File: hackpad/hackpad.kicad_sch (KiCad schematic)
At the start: 23 parts, among them J1 Conn_01x04_Pin, SW1 SW_Push_45deg, SW10 RotaryEncoder_Switch, SW11 RotaryEncoder_Switch, SW2 SW_Push_45deg, SW3 SW_Push_45deg, SW4 SW_Push_45deg, SW5 SW_Push_45deg, SW6 SW_Push_45deg, SW7 SW_Push_45deg, SW8 SW_Push_45deg, SW9 SW_Push_45deg, U1 MOUDLE-SEEEDUINO-XIAO, U2 ER_OLEDM0.91_1x-I2C

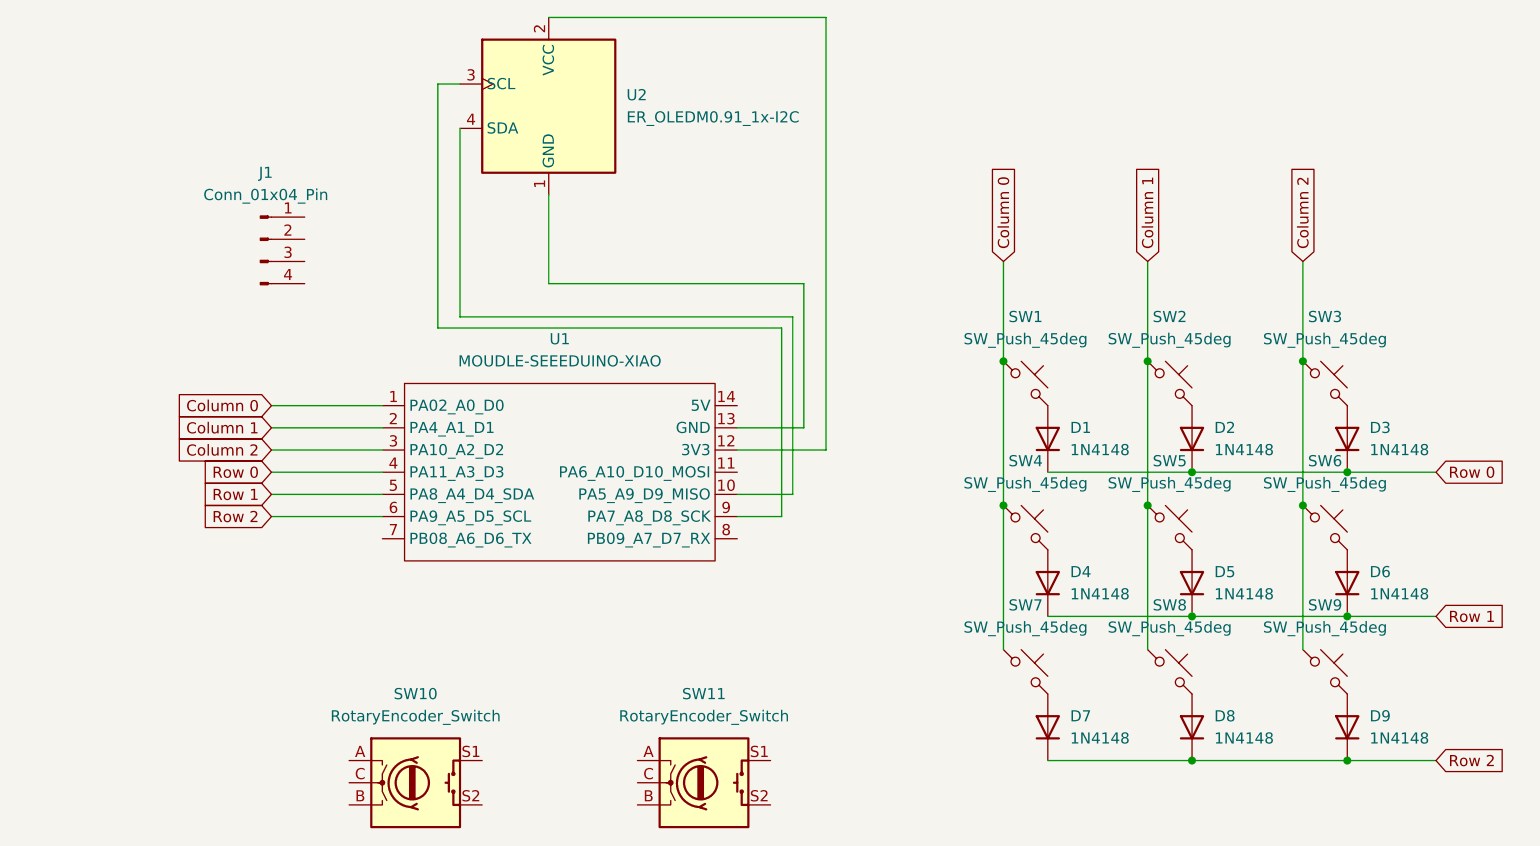
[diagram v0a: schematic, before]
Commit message: Schematic Complete
Schematic complete currently routing
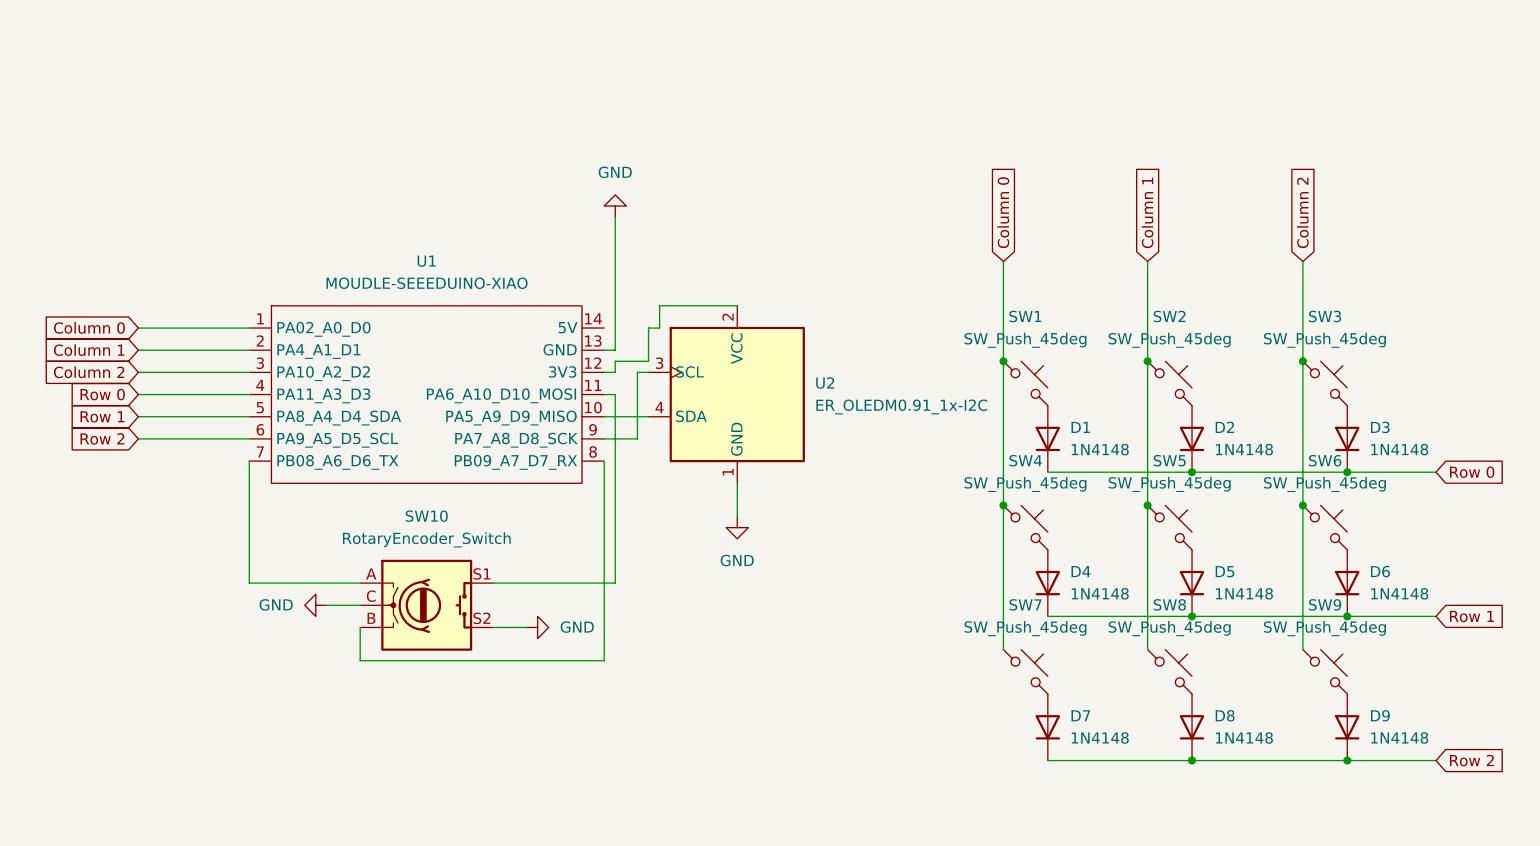
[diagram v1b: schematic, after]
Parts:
- removed J1: Conn_01x04_Pin, Display:ER_OLEDM0.91_1x-I2C, symbol Connector:Conn_01x04_Pin
- removed SW11: RotaryEncoder_Switch, symbol Device:RotaryEncoder_Switch
- SW10: footprint Package_SO:TSSOP-16_4.4x5mm_P0.65mm -> Rotary_Encoder:RotaryEncoder_Alps_EC11E-Switch_Vertical_H20mm
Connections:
- net at U1.11 (PA6_A10_D10_MOSI): now also SW10.S1
- net GND: now reaches U1.13 (GND), U2.1 (GND)
- net GND: now also SW10.C, SW10.S2
- net at U1.7 (PB08_A6_D6_TX): now also SW10.A
- net at U1.8 (PB09_A7_D7_RX): now also SW10.B
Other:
- moved on the sheet: SW10, U1, U2

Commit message: rotated XIAO
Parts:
- removed SW10: RotaryEncoder_Switch, Rotary_Encoder:RotaryEncoder_Alps_EC11E-Switch_Vertical_H20mm, symbol Device:RotaryEncoder_Switch
- added SW10: RotaryEncoder_Switch_MP, Rotary_Encoder:RotaryEncoder_Alps_EC11E-Switch_Vertical_H20mm, symbol Device:RotaryEncoder_Switch_MP
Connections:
- net GND: now also SW10.C, SW10.MP, SW10.S2
- net at U1.11 (PA6_A10_D10_MOSI): now also SW10.S1
- net at U1.7 (PB08_A6_D6_TX): now also SW10.A
- net at U1.8 (PB09_A7_D7_RX): now also SW10.B
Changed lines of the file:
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@@
+	(wire
+		(pts
+			(xy 59.69 133.35) (xy 59.69 138.43)
+		)
+		(stroke
+			(width 0)
+			(type default)
+		)
+	)
 	(wire
 		(pts
@@
 	)
 	(symbol
+		(lib_id "Device:RotaryEncoder_Switch_MP")
+		(at 59.69 125.73 0)
+		(unit 1)
+		(body_style 1)
+		(exclude_from_sim no)
+		(in_bom yes)
+		(on_board yes)
+		(in_pos_files yes)
+		(dnp no)
+		(fields_autoplaced yes)
+		(property "Reference" "SW10"
+			(at 59.69 115.57 0)
+			(show_name no)
+			(do_not_autoplace no)
+			(effects
+				(font
+					(size 1.27 1.27)
+				)
+			)
+		)
+		(property "Value" "RotaryEncoder_Switch_MP"
+			(at 59.69 118.11 0)
+			(show_name no)
+			(do_not_autoplace no)
+			(effects
+				(font
+					(size 1.27 1.27)
+				)
+			)
+		)
+		(property "Footprint" "Rotary_Encoder:RotaryEncoder_Alps_EC11E-Switch_Vertical_H20mm"
+			(at 55.88 121.666 0)
+			(hide yes)
+			(show_name no)
+			(do_not_autoplace no)
+			(effects
+				(font
+					(size 1.27 1.27)
+				)
+			)
+		)
+		(property "Datasheet" ""
+			(at 59.69 138.43 0)
+			(hide yes)
+			(show_name no)
+			(do_not_autoplace no)
+			(effects
+				(font
+					(size 1.27 1.27)
+				)
+			)
+		)
+		(property "Description" "Rotary encoder, dual channel, incremental quadrate outputs, with switch and MP Pin"
+			(at 59.69 140.97 0)
+			(hide yes)
+			(show_name no)
+			(do_not_autoplace no)
+			(effects
+				(font
+					(size 1.27 1.27)
+				)
+			)
+		)
+		(pin "S1"
+		)
+		(pin "A"
+		)
+		(pin "C"
+		)
+		(pin "MP"
+		)
+		(pin "B"
+		)
+		(pin "S2"
+		)
+		(instances
+			(project "hackpad"
+				(path "/b28a3658-46e1-46bb-8f99-59dd27d671e5"
+					(reference "SW10")
+					(unit 1)
+				)
+			)
+		)
+	)
+	(symbol
 		(lib_id "XIAO_RP2040:MOUDLE-SEEEDUINO-XIAO")
 		(at 58.42 101.6 0)
@@
 	)
 	(symbol
+		(lib_id "power:GND")
+		(at 59.69 138.43 0)
+		(unit 1)
+		(body_style 1)
+		(exclude_from_sim no)
+		(in_bom yes)
+		(on_board yes)
+		(in_pos_files yes)
+		(dnp no)
+		(fields_autoplaced yes)
+		(property "Reference" "#PWR05"
+			(at 59.69 144.78 0)
+			(hide yes)
+			(show_name no)
+			(do_not_autoplace no)
+			(effects
+				(font
+					(size 1.27 1.27)
+				)
+			)
+		)
+		(property "Value" "GND"
+			(at 59.69 143.51 0)
+			(show_name no)
+			(do_not_autoplace no)
+			(effects
+				(font
+					(size 1.27 1.27)
+				)
+			)
+		)
+		(property "Footprint" ""
+			(at 59.69 138.43 0)
+			(hide yes)
+			(show_name no)
+			(do_not_autoplace no)
+			(effects
+				(font
+					(size 1.27 1.27)
+				)
+			)
+		)
+		(property "Datasheet" ""
+			(at 59.69 138.43 0)
+			(hide yes)
+			(show_name no)
+			(do_not_autoplace no)
+			(effects
+				(font
+					(size 1.27 1.27)
+				)
+			)
+		)
+		(property "Description" "Power symbol creates a global label with name \"GND\" , ground"
+			(at 59.69 138.43 0)
+			(hide yes)
+			(show_name no)
+			(do_not_autoplace no)
+			(effects
+				(font
+					(size 1.27 1.27)
+				)
+			)
+		)
+		(pin "1"
+		)
+		(instances
+			(project "hackpad"
+				(path "/b28a3658-46e1-46bb-8f99-59dd27d671e5"
+					(reference "#PWR05")
+					(unit 1)
+				)
+			)
+		)
+	)
+	(symbol
 		(lib_id "Switch:SW_Push_45deg")
 		(at 144.78 116.84 0)
@@
 					(unit 1)
 				)
-			)
-		)
-	)
-	(symbol
-		(lib_id "Device:RotaryEncoder_Switch")
-		(at 59.69 125.73 0)
-		(unit 1)
-		(body_style 1)
-		(exclude_from_sim no)
-		(in_bom yes)
-		(on_board yes)
-		(in_pos_files yes)
-		(dnp no)
-		(fields_autoplaced yes)
-		(property "Reference" "SW10"
-			(at 59.69 115.57 0)
-			(show_name no)
-			(do_not_autoplace no)
-			(effects
-				(font
-					(size 1.27 1.27)
-				)
-			)
-		)
-		(property "Value" "RotaryEncoder_Switch"
-			(at 59.69 118.11 0)
-			(show_name no)
-			(do_not_autoplace no)
-			(effects
-				(font
-					(size 1.27 1.27)
-				)
-			)
-		)
-		(property "Footprint" "Rotary_Encoder:RotaryEncoder_Alps_EC11E-Switch_Vertical_H20mm"
-			(at 55.88 121.666 0)
-			(hide yes)
-			(show_name no)
-			(do_not_autoplace no)
-			(effects
-				(font
-					(size 1.27 1.27)
-				)
-			)
-		)
-		(property "Datasheet" ""
-			(at 59.69 119.126 0)
-			(hide yes)
-			(show_name no)
-			(do_not_autoplace no)
-			(effects
-				(font
-					(size 1.27 1.27)
-				)
-			)
-		)
-		(property "Description" "Rotary encoder, dual channel, incremental quadrate outputs, with switch"
-			(at 59.69 125.73 0)
-			(hide yes)
-			(show_name no)
-			(do_not_autoplace no)
-			(effects
-				(font
-					(size 1.27 1.27)
-				)
-			)
-		)
-		(pin "A"
-		)
-		(pin "C"
-		)
-		(pin "S1"
-		)
-		(pin "B"
-		)
-		(pin "S2"
-		)
-		(instances
-			(project "hackpad"
-				(path "/b28a3658-46e1-46bb-8f99-59dd27d671e5"
-					(reference "SW10")
-					(unit 1)
-				)
